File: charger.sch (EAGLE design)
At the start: 12 parts

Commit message: Fixed inductor footprint, updated layout
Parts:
- removed L1: 1uH, Coilcraft:XFL4020
- added U$3: SRU1028, ti:SRU1028
- C1: device adafruit:C-USC0603K -> resistor:C-USC1206
- C3: value 18pF -> 18 pF; device adafruit:C-USC0603K -> resistor:C-USC0603K
- C4, C5, C6: device adafruit:C-USC0603K -> resistor:C-USC0805K
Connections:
- net IND: now also U$3.2; no longer L1.2
- net VIN: now also U$3.1; no longer L1.1
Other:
- note added: "1 uF"
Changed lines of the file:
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@@
 <parts>
 <part name="U$1" library="texas" deviceset="TPS61230" device=""/>
-<part name="L1" library="Coilcraft" deviceset="XFL4020" device="" value="1uH"/>
-<part name="C1" library="adafruit" deviceset="C-US" device="C0603K" value="22uF"/>
 <part name="SUPPLY1" library="supply2" deviceset="GND" device=""/>
 <part name="C2" library="adafruit" deviceset="C-US" device="C0603K" value="150nF"/>
@@
 <part name="R2" library="adafruit" deviceset="R-US_" device="R0603" value="100k"/>
 <part name="SUPPLY3" library="supply2" deviceset="GND" device=""/>
-<part name="C3" library="adafruit" deviceset="C-US" device="C0603K" value="18pF"/>
-<part name="C4" library="adafruit" deviceset="C-US" device="C0603K" value="10uF"/>
 <part name="SUPPLY4" library="supply2" deviceset="GND" device=""/>
 <part name="SUPPLY5" library="supply2" deviceset="GND" device=""/>
-<part name="C5" library="adafruit" deviceset="C-US" device="C0603K" value="10uF"/>
-<part name="C6" library="adafruit" deviceset="C-US" device="C0603K" value="10uF"/>
 <part name="SUPPLY6" library="supply2" deviceset="GND" device=""/>
 <part name="SUPPLY7" library="supply2" deviceset="GND" device=""/>
@@
 <part name="U$2" library="ti" deviceset="USB-VERT" device=""/>
 <part name="SUPPLY8" library="supply2" deviceset="GND" device=""/>
+<part name="U$3" library="ti" deviceset="SRU1028" device=""/>
+<part name="C3" library="resistor" deviceset="C-US" device="C0603K" value="18 pF"/>
+<part name="C1" library="resistor" deviceset="C-US" device="C1206" value="22uF"/>
+<part name="C6" library="resistor" deviceset="C-US" device="C0805K" value="10uF"/>
+<part name="C5" library="resistor" deviceset="C-US" device="C0805K" value="10uF"/>
+<part name="C4" library="resistor" deviceset="C-US" device="C0805K" value="10uF"/>
 </parts>
 <sheets>
 <sheet>
 <plain>
+<text x="-2.54" y="17.78" size="1.778" layer="96">1 uF</text>
 </plain>
 <instances>
 <instance part="U$1" gate="G$1" x="0" y="0"/>
-<instance part="L1" gate="L$1" x="0" y="20.32"/>
-<instance part="C1" gate="G$1" x="-33.02" y="5.08"/>
 <instance part="SUPPLY1" gate="GND" x="-33.02" y="-5.08"/>
 <instance part="C2" gate="G$1" x="-20.32" y="-7.62"/>
@@
 </instance>
 <instance part="SUPPLY3" gate="GND" x="30.48" y="-27.94"/>
-<instance part="C3" gate="G$1" x="22.86" y="0" smashed="yes">
-<attribute name="NAME" x="18.796" y="3.175" size="1.778" layer="95"/>
-<attribute name="VALUE" x="16.256" y="0.889" size="1.778" layer="96"/>
-</instance>
-<instance part="C4" gate="G$1" x="48.26" y="0"/>
 <instance part="SUPPLY4" gate="GND" x="48.26" y="-12.7"/>
 <instance part="SUPPLY5" gate="GND" x="-50.8" y="0"/>
-<instance part="C5" gate="G$1" x="58.42" y="0"/>
-<instance part="C6" gate="G$1" x="68.58" y="0"/>
 <instance part="SUPPLY6" gate="GND" x="58.42" y="-12.7"/>
 <instance part="SUPPLY7" gate="GND" x="68.58" y="-12.7"/>
@@
 <instance part="U$2" gate="G$1" x="99.06" y="-7.62"/>
 <instance part="SUPPLY8" gate="GND" x="93.98" y="-12.7"/>
+<instance part="U$3" gate="G$1" x="-10.16" y="20.32" smashed="yes"/>
+<instance part="C3" gate="G$1" x="22.86" y="0" smashed="yes">
+<attribute name="NAME" x="23.876" y="0.635" size="1.778" layer="95"/>
+<attribute name="VALUE" x="16.256" y="0.889" size="1.778" layer="96"/>
+</instance>
+<instance part="C1" gate="G$1" x="-33.02" y="5.08"/>
+<instance part="C6" gate="G$1" x="68.58" y="0"/>
+<instance part="C5" gate="G$1" x="58.42" y="0"/>
+<instance part="C4" gate="G$1" x="48.26" y="0"/>
 </instances>
 <busses>
@@
 <wire x1="12.7" y1="10.16" x2="15.24" y2="10.16" width="0.1524" layer="91"/>
 <wire x1="15.24" y1="10.16" x2="15.24" y2="20.32" width="0.1524" layer="91"/>
-<pinref part="L1" gate="L$1" pin="2"/>
-<wire x1="15.24" y1="20.32" x2="7.62" y2="20.32" width="0.1524" layer="91"/>
+<pinref part="U$3" gate="G$1" pin="2"/>
+<wire x1="7.62" y1="20.32" x2="15.24" y2="20.32" width="0.1524" layer="91"/>
 </segment>
 </net>
 <net name="VIN" class="0">
 <segment>
-<pinref part="L1" gate="L$1" pin="1"/>
-<wire x1="-7.62" y1="20.32" x2="-15.24" y2="20.32" width="0.1524" layer="91"/>
 <wire x1="-15.24" y1="20.32" x2="-15.24" y2="10.16" width="0.1524" layer="91"/>
 <pinref part="U$1" gate="G$1" pin="VIN"/>
@@
 <wire x1="-15.24" y1="10.16" x2="-33.02" y2="10.16" width="0.1524" layer="91"/>
 <junction x="-15.24" y="10.16"/>
-<pinref part="C1" gate="G$1" pin="1"/>
 <wire x1="-33.02" y1="7.62" x2="-33.02" y2="10.16" width="0.1524" layer="91"/>
 <pinref part="U$1" gate="G$1" pin="EN"/>
@@
 <wire x1="-58.42" y1="10.16" x2="-33.02" y2="10.16" width="0.1524" layer="91"/>
 <pinref part="JP1" gate="G$1" pin="2"/>
+<pinref part="U$3" gate="G$1" pin="1"/>
+<wire x1="-15.24" y1="20.32" x2="-7.62" y2="20.32" width="0.1524" layer="91"/>
+<pinref part="C1" gate="G$1" pin="1"/>
 </segment>
 </net>
 <net name="GND" class="0">
 <segment>
-<pinref part="C1" gate="G$1" pin="2"/>
 <pinref part="SUPPLY1" gate="GND" pin="GND"/>
 <wire x1="-33.02" y1="0" x2="-33.02" y2="-2.54" width="0.1524" layer="91"/>
+<pinref part="C1" gate="G$1" pin="2"/>
 </segment>
 <segment>
@@
 </segment>
 <segment>
-<pinref part="C4" gate="G$1" pin="2"/>
 <pinref part="SUPPLY4" gate="GND" pin="GND"/>
 <wire x1="48.26" y1="-10.16" x2="48.26" y2="-5.08" width="0.1524" layer="91"/>
+<pinref part="C4" gate="G$1" pin="2"/>
 </segment>
 <segment>
-<pinref part="C5" gate="G$1" pin="2"/>
 <pinref part="SUPPLY6" gate="GND" pin="GND"/>
 <wire x1="58.42" y1="-5.08" x2="58.42" y2="-10.16" width="0.1524" layer="91"/>
+<pinref part="C5" gate="G$1" pin="2"/>
 </segment>
 <segment>
-<pinref part="C6" gate="G$1" pin="2"/>
 <pinref part="SUPPLY7" gate="GND" pin="GND"/>
 <wire x1="68.58" y1="-5.08" x2="68.58" y2="-10.16" width="0.1524" layer="91"/>
+<pinref part="C6" gate="G$1" pin="2"/>
 </segment>
 <segment>
@@
 <wire x1="30.48" y1="2.54" x2="30.48" y2="5.08" width="0.1524" layer="91"/>
 <junction x="30.48" y="5.08"/>
-<pinref part="C4" gate="G$1" pin="1"/>
 <wire x1="48.26" y1="2.54" x2="48.26" y2="5.08" width="0.1524" layer="91"/>
 <junction x="48.26" y="5.08"/>
 <wire x1="93.98" y1="5.08" x2="68.58" y2="5.08" width="0.1524" layer="91"/>
-<pinref part="C3" gate="G$1" pin="1"/>
 <wire x1="68.58" y1="5.08" x2="58.42" y2="5.08" width="0.1524" layer="91"/>
 <wire x1="58.42" y1="5.08" x2="48.26" y2="5.08" width="0.1524" layer="91"/>
 <wire x1="22.86" y1="2.54" x2="22.86" y2="5.08" width="0.1524" layer="91"/>
 <junction x="22.86" y="5.08"/>
-<pinref part="C5" gate="G$1" pin="1"/>
 <wire x1="58.42" y1="2.54" x2="58.42" y2="5.08" width="0.1524" layer="91"/>
-<pinref part="C6" gate="G$1" pin="1"/>
 <wire x1="68.58" y1="2.54" x2="68.58" y2="5.08" width="0.1524" layer="91"/>
 <junction x="58.42" y="5.08"/>
 <junction x="68.58" y="5.08"/>
 <pinref part="U$2" gate="G$1" pin="VCC"/>
+<pinref part="C3" gate="G$1" pin="1"/>
+<pinref part="C4" gate="G$1" pin="1"/>
+<pinref part="C5" gate="G$1" pin="1"/>
+<pinref part="C6" gate="G$1" pin="1"/>
 </segment>
 </net>
@@
 <wire x1="17.78" y1="-7.62" x2="22.86" y2="-7.62" width="0.1524" layer="91"/>
 <junction x="30.48" y="-7.62"/>
-<pinref part="C3" gate="G$1" pin="2"/>
 <wire x1="22.86" y1="-7.62" x2="30.48" y2="-7.62" width="0.1524" layer="91"/>
 <wire x1="22.86" y1="-5.08" x2="22.86" y2="-7.62" width="0.1524" layer="91"/>
 <junction x="22.86" y="-7.62"/>
+<pinref part="C3" gate="G$1" pin="2"/>
 </segment>
 </net>

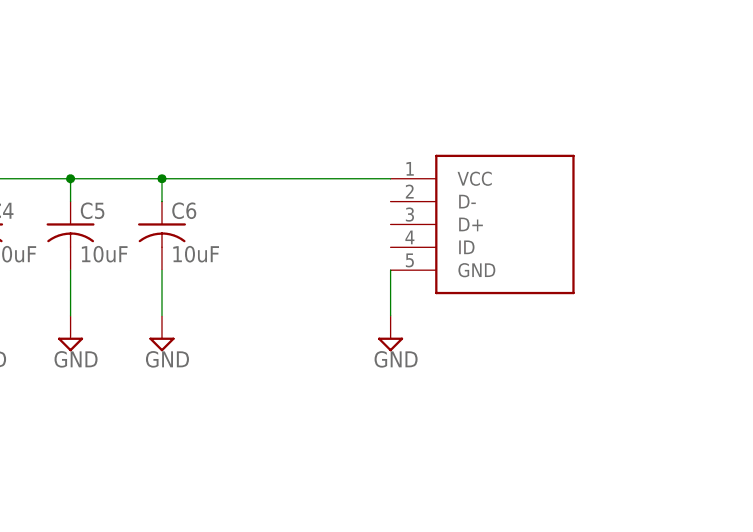
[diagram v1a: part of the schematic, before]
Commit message: Fixed dimensions and updated USB connector
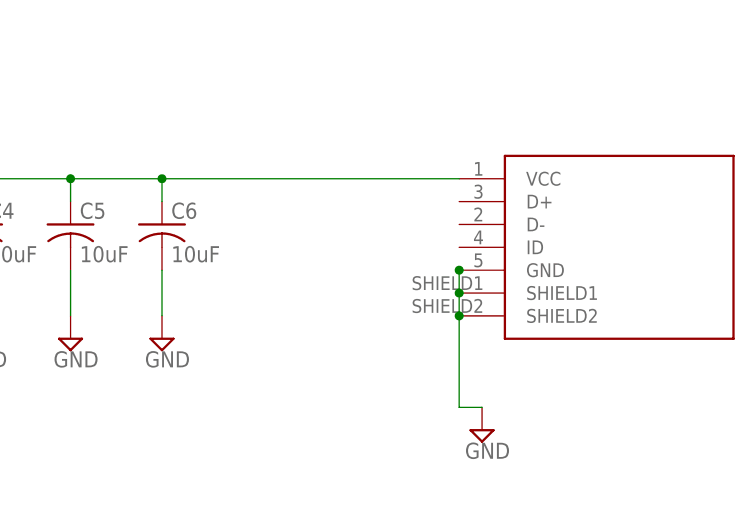
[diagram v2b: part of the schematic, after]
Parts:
- removed U$2: USB-VERT, ti:USB-VERT
- added U$4: USB2, ti:USB2
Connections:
- net GND: now also U$4.GND, U$4.SHIELD1, U$4.SHIELD2; no longer U$2.GND
- net VOUT: now also U$4.VCC; no longer U$2.VCC
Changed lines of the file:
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@@
 <part name="SUPPLY7" library="supply2" deviceset="GND" device=""/>
 <part name="JP1" library="SparkFun-Connectors" deviceset="M02" device="PTH"/>
-<part name="U$2" library="ti" deviceset="USB-VERT" device=""/>
 <part name="SUPPLY8" library="supply2" deviceset="GND" device=""/>
 <part name="U$3" library="ti" deviceset="SRU1028" device=""/>
@@
 <part name="C5" library="resistor" deviceset="C-US" device="C0805K" value="10uF"/>
 <part name="C4" library="resistor" deviceset="C-US" device="C0805K" value="10uF"/>
+<part name="U$4" library="ti" deviceset="USB2" device=""/>
 </parts>
 <sheets>
@@
 <instance part="SUPPLY7" gate="GND" x="68.58" y="-12.7"/>
 <instance part="JP1" gate="G$1" x="-66.04" y="7.62"/>
-<instance part="U$2" gate="G$1" x="99.06" y="-7.62"/>
-<instance part="SUPPLY8" gate="GND" x="93.98" y="-12.7"/>
+<instance part="SUPPLY8" gate="GND" x="104.14" y="-22.86"/>
 <instance part="U$3" gate="G$1" x="-10.16" y="20.32" smashed="yes"/>
 <instance part="C3" gate="G$1" x="22.86" y="0" smashed="yes">
@@
 <instance part="C5" gate="G$1" x="58.42" y="0"/>
 <instance part="C4" gate="G$1" x="48.26" y="0"/>
+<instance part="U$4" gate="G$1" x="106.68" y="-12.7"/>
 </instances>
 <busses>
@@
 </segment>
 <segment>
-<pinref part="U$2" gate="G$1" pin="GND"/>
+<pinref part="U$4" gate="G$1" pin="GND"/>
+<pinref part="U$4" gate="G$1" pin="SHIELD1"/>
+<wire x1="101.6" y1="-5.08" x2="101.6" y2="-7.62" width="0.1524" layer="91"/>
+<pinref part="U$4" gate="G$1" pin="SHIELD2"/>
+<wire x1="101.6" y1="-7.62" x2="101.6" y2="-10.16" width="0.1524" layer="91"/>
+<wire x1="101.6" y1="-10.16" x2="101.6" y2="-20.32" width="0.1524" layer="91"/>
 <pinref part="SUPPLY8" gate="GND" pin="GND"/>
-<wire x1="93.98" y1="-5.08" x2="93.98" y2="-10.16" width="0.1524" layer="91"/>
+<wire x1="101.6" y1="-20.32" x2="104.14" y2="-20.32" width="0.1524" layer="91"/>
+<junction x="101.6" y="-10.16"/>
+<junction x="101.6" y="-7.62"/>
+<junction x="101.6" y="-5.08"/>
 </segment>
 </net>
@@
 <wire x1="48.26" y1="2.54" x2="48.26" y2="5.08" width="0.1524" layer="91"/>
 <junction x="48.26" y="5.08"/>
-<wire x1="93.98" y1="5.08" x2="68.58" y2="5.08" width="0.1524" layer="91"/>
+<wire x1="101.6" y1="5.08" x2="68.58" y2="5.08" width="0.1524" layer="91"/>
 <wire x1="68.58" y1="5.08" x2="58.42" y2="5.08" width="0.1524" layer="91"/>
 <wire x1="58.42" y1="5.08" x2="48.26" y2="5.08" width="0.1524" layer="91"/>
@@
 <junction x="58.42" y="5.08"/>
 <junction x="68.58" y="5.08"/>
-<pinref part="U$2" gate="G$1" pin="VCC"/>
 <pinref part="C3" gate="G$1" pin="1"/>
 <pinref part="C4" gate="G$1" pin="1"/>
 <pinref part="C5" gate="G$1" pin="1"/>
 <pinref part="C6" gate="G$1" pin="1"/>
+<pinref part="U$4" gate="G$1" pin="VCC"/>
 </segment>
 </net>
